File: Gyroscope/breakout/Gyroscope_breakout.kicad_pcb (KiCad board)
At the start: 2 copper layers, 30 x 22.9 mm, 5 parts, among them IC101 BMI088, J101 Conn_01x08

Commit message: Updated post review
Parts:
- C101, C102: footprint Gyroscope:C_0201_0603Metric -> Gyroscope:C_0805_2012Metric_Pad1.15x1.40mm_HandSolder
- moved C102 3.00 mm to (132.0, 98.1), turned to 0 degrees
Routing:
- net +3V3: track 32.8 -> 34.6 mm, vias 1 -> 2

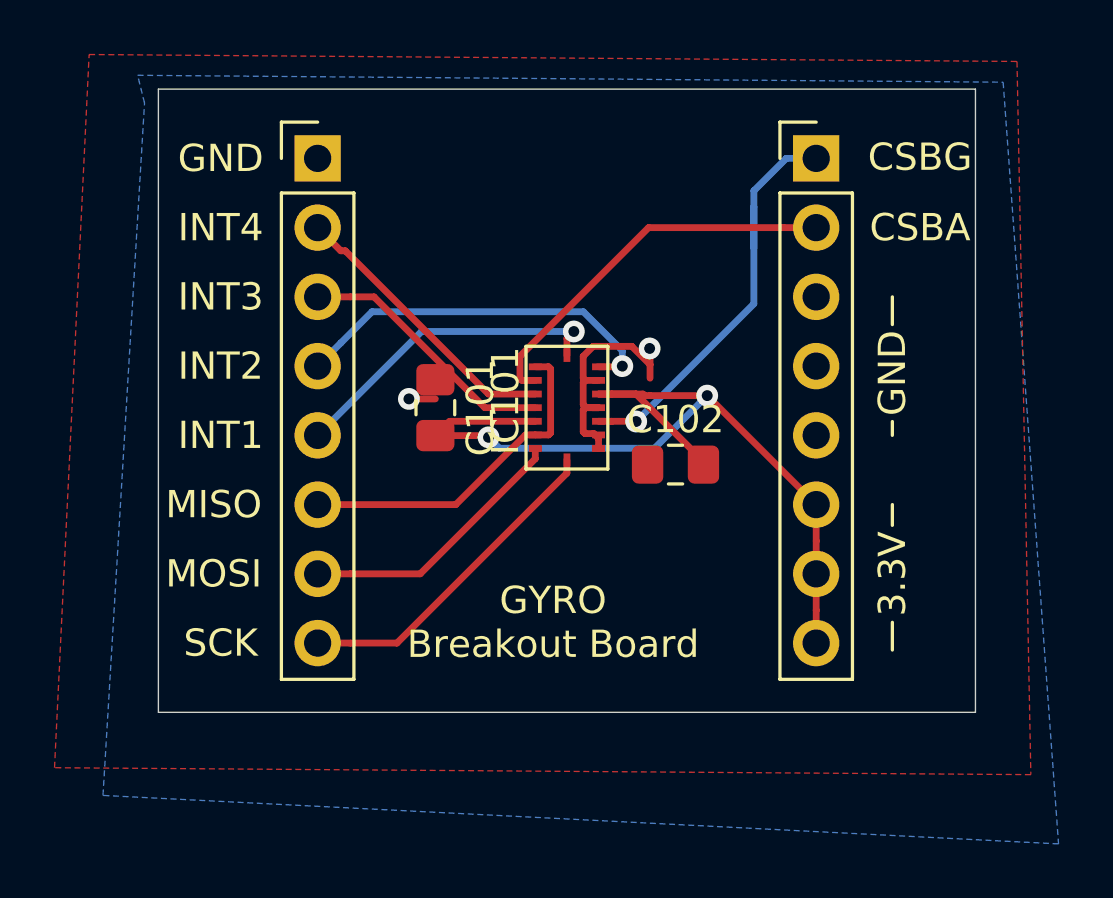
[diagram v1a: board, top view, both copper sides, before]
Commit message: Minor routing fix
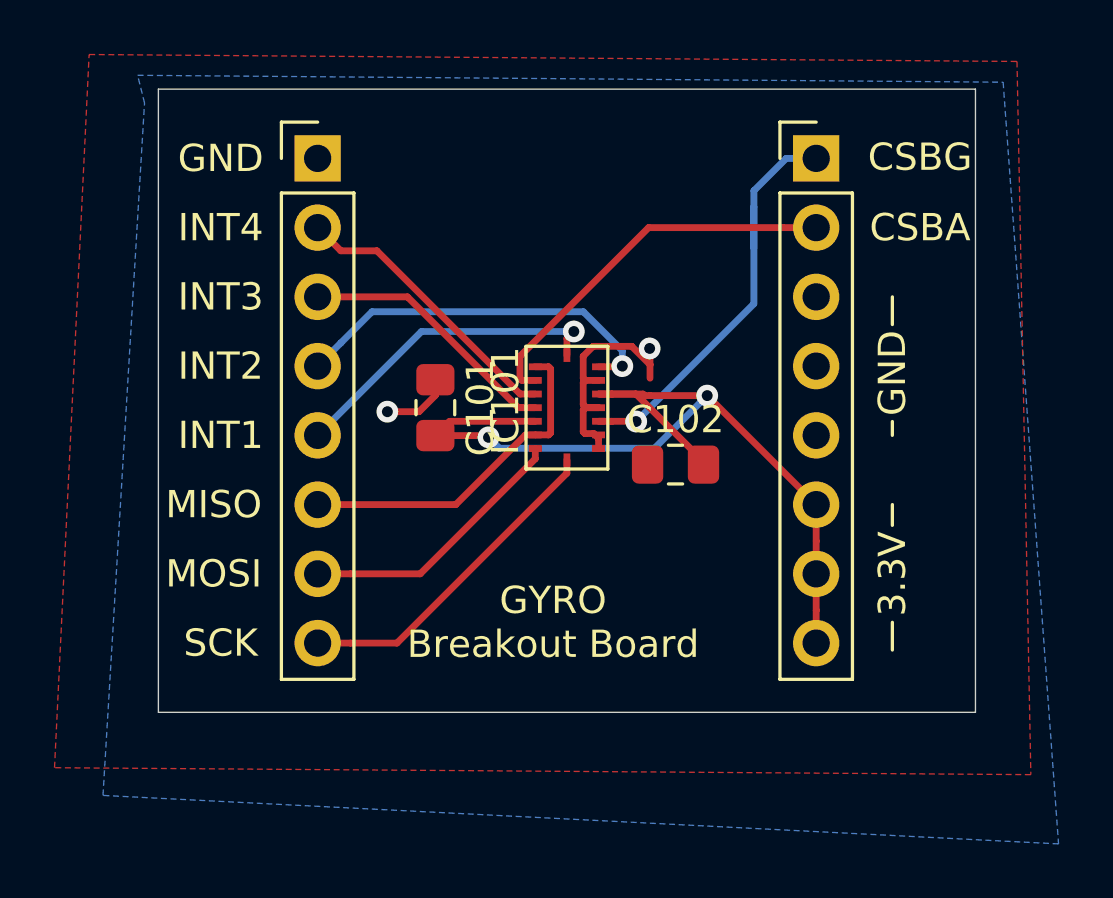
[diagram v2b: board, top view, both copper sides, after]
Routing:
- net GND: track 10.3 -> 11.9 mm
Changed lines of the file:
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@@
     (thickness 1.6)
     (drawings 21)
-    (tracks 99)
+    (tracks 100)
     (zones 0)
     (modules 5)
@@
   )
   (module Gyroscope:C_0805_2012Metric_Pad1.15x1.40mm_HandSolder (layer F.Cu)
+    (at 123.19 96.012 270)
+    (descr "Capacitor SMD 0805 (2012 Metric), square (rectangular) end terminal, IPC_7351 nominal with elongated pad for handsoldering. (Body size source: https://docs.google.com/spreadsheets/d/1BsfQQcO9C6DZCsRaXUlFlo91Tg2WpOkGARC1WS5S8t0/edit?usp=sharing), generated with kicad-footprint-generator")
+    (tags "capacitor handsolder")
+    (attr smd)
+    (fp_text reference C101 (at 0 -1.65 90) (layer F.SilkS)
+      (effects (font (size 1 1) (thickness 0.15)))
+    )
+    (fp_text value 100nF (at 0 1.65 90) (layer F.Fab)
+      (effects (font (size 1 1) (thickness 0.15)))
+    )
+    (fp_text user %R (at 0 0 90) (layer F.Fab)
+      (effects (font (size 0.5 0.5) (thickness 0.08)))
+    )
+    (fp_line (start 1.85 0.95) (end -1.85 0.95) (layer F.CrtYd) (width 0.05))
+    (fp_line (start 1.85 -0.95) (end 1.85 0.95) (layer F.CrtYd) (width 0.05))
+    (fp_line (start -1.85 -0.95) (end 1.85 -0.95) (layer F.CrtYd) (width 0.05))
+    (fp_line (start -1.85 0.95) (end -1.85 -0.95) (layer F.CrtYd) (width 0.05))
+    (fp_line (start -0.261252 0.71) (end 0.261252 0.71) (layer F.SilkS) (width 0.12))
+    (fp_line (start -0.261252 -0.71) (end 0.261252 -0.71) (layer F.SilkS) (width 0.12))
+    (fp_line (start 1 0.6) (end -1 0.6) (layer F.Fab) (width 0.1))
+    (fp_line (start 1 -0.6) (end 1 0.6) (layer F.Fab) (width 0.1))
+    (fp_line (start -1 -0.6) (end 1 -0.6) (layer F.Fab) (width 0.1))
+    (fp_line (start -1 0.6) (end -1 -0.6) (layer F.Fab) (width 0.1))
+    (pad 2 smd roundrect (at 1.025 0 270) (size 1.15 1.4) (layers F.Cu F.Paste F.Mask) (roundrect_rratio 0.217391)
+      (net 2 +3V3))
+    (pad 1 smd roundrect (at -1.025 0 270) (size 1.15 1.4) (layers F.Cu F.Paste F.Mask) (roundrect_rratio 0.217391)
+      (net 1 GND))
+    (model ${KISYS3DMOD}/Capacitor_SMD.3dshapes/C_0805_2012Metric.wrl
+      (at (xyz 0 0 0))
+      (scale (xyz 1 1 1))
+      (rotate (xyz 0 0 0))
+    )
+  )
+  (module Gyroscope:C_0805_2012Metric_Pad1.15x1.40mm_HandSolder (layer F.Cu)
     (at 132 98.1)
     (descr "Capacitor SMD 0805 (2012 Metric), square (rectangular) end terminal, IPC_7351 nominal with elongated pad for handsoldering. (Body size source: https://docs.google.com/spreadsheets/d/1BsfQQcO9C6DZCsRaXUlFlo91Tg2WpOkGARC1WS5S8t0/edit?usp=sharing), generated with kicad-footprint-generator")
@@
       (net 2 +3V3))
     (pad 1 smd roundrect (at -1.025 0) (size 1.15 1.4) (layers F.Cu F.Paste F.Mask) (roundrect_rratio 0.217391)
-      (net 1 GND))
-    (model ${KISYS3DMOD}/Capacitor_SMD.3dshapes/C_0805_2012Metric.wrl
-      (at (xyz 0 0 0))
-      (scale (xyz 1 1 1))
-      (rotate (xyz 0 0 0))
-    )
-  )
-  (module Gyroscope:C_0805_2012Metric_Pad1.15x1.40mm_HandSolder (layer F.Cu)
-    (at 123.19 96.012 270)
-    (descr "Capacitor SMD 0805 (2012 Metric), square (rectangular) end terminal, IPC_7351 nominal with elongated pad for handsoldering. (Body size source: https://docs.google.com/spreadsheets/d/1BsfQQcO9C6DZCsRaXUlFlo91Tg2WpOkGARC1WS5S8t0/edit?usp=sharing), generated with kicad-footprint-generator")
-    (tags "capacitor handsolder")
-    (attr smd)
-    (fp_text reference C101 (at 0 -1.65 90) (layer F.SilkS)
-      (effects (font (size 1 1) (thickness 0.15)))
-    )
-    (fp_text value 100nF (at 0 1.65 90) (layer F.Fab)
-      (effects (font (size 1 1) (thickness 0.15)))
-    )
-    (fp_text user %R (at 0 0 90) (layer F.Fab)
-      (effects (font (size 0.5 0.5) (thickness 0.08)))
-    )
-    (fp_line (start 1.85 0.95) (end -1.85 0.95) (layer F.CrtYd) (width 0.05))
-    (fp_line (start 1.85 -0.95) (end 1.85 0.95) (layer F.CrtYd) (width 0.05))
-    (fp_line (start -1.85 -0.95) (end 1.85 -0.95) (layer F.CrtYd) (width 0.05))
-    (fp_line (start -1.85 0.95) (end -1.85 -0.95) (layer F.CrtYd) (width 0.05))
-    (fp_line (start -0.261252 0.71) (end 0.261252 0.71) (layer F.SilkS) (width 0.12))
-    (fp_line (start -0.261252 -0.71) (end 0.261252 -0.71) (layer F.SilkS) (width 0.12))
-    (fp_line (start 1 0.6) (end -1 0.6) (layer F.Fab) (width 0.1))
-    (fp_line (start 1 -0.6) (end 1 0.6) (layer F.Fab) (width 0.1))
-    (fp_line (start -1 -0.6) (end 1 -0.6) (layer F.Fab) (width 0.1))
-    (fp_line (start -1 0.6) (end -1 -0.6) (layer F.Fab) (width 0.1))
-    (pad 2 smd roundrect (at 1.025 0 270) (size 1.15 1.4) (layers F.Cu F.Paste F.Mask) (roundrect_rratio 0.217391)
-      (net 2 +3V3))
-    (pad 1 smd roundrect (at -1.025 0 270) (size 1.15 1.4) (layers F.Cu F.Paste F.Mask) (roundrect_rratio 0.217391)
       (net 1 GND))
     (model ${KISYS3DMOD}/Capacitor_SMD.3dshapes/C_0805_2012Metric.wrl
@@
   (segment (start 131.064 94.430998) (end 131.064 93.854) (width 0.25) (layer F.Cu) (net 1))
   (segment (start 131.064 93.854) (end 131.05 93.84) (width 0.25) (layer F.Cu) (net 1))
-  (segment (start 122.222 95.692) (end 122.22 95.69) (width 0.25) (layer F.Cu) (net 1))
-  (via (at 122.22 95.69) (size 0.8) (drill 0.4) (layers F.Cu B.Cu) (net 1))
-  (segment (start 123.19 95.692) (end 122.222 95.692) (width 0.25) (layer F.Cu) (net 1) (status 10))
+  (via (at 121.43 96.16) (size 0.8) (drill 0.4) (layers F.Cu B.Cu) (net 1))
+  (segment (start 122.592 96.16) (end 121.43 96.16) (width 0.25) (layer F.Cu) (net 1))
+  (segment (start 123.19 94.987) (end 123.19 95.562) (width 0.25) (layer F.Cu) (net 1))
+  (segment (start 123.19 95.562) (end 122.592 96.16) (width 0.25) (layer F.Cu) (net 1))
   (segment (start 130.806 95.512) (end 129.176 95.512) (width 0.25) (layer F.Cu) (net 2) (status 20))
   (segment (start 131.064 95.57) (end 130.864 95.57) (width 0.25) (layer F.Cu) (net 2) (status 30))
@@
   (segment (start 126.494178 97.012) (end 126.856 97.012) (width 0.25) (layer F.Cu) (net 7))
   (segment (start 118.872 99.568) (end 123.938178 99.568) (width 0.25) (layer F.Cu) (net 7))
-  (segment (start 120.940002 91.948) (end 120.074081 91.948) (width 0.25) (layer F.Cu) (net 8))
-  (segment (start 125.004002 96.012) (end 120.940002 91.948) (width 0.25) (layer F.Cu) (net 8))
-  (segment (start 120.074081 91.948) (end 118.872 91.948) (width 0.25) (layer F.Cu) (net 8) (status 20))
-  (segment (start 126.856 96.012) (end 125.004002 96.012) (width 0.25) (layer F.Cu) (net 8) (status 10))
-  (segment (start 119.721999 90.257999) (end 118.872 89.408) (width 0.25) (layer F.Cu) (net 9) (status 20))
-  (segment (start 125.140412 95.512) (end 119.886411 90.257999) (width 0.25) (layer F.Cu) (net 9))
-  (segment (start 119.886411 90.257999) (end 119.721999 90.257999) (width 0.25) (layer F.Cu) (net 9))
-  (segment (start 126.856 95.512) (end 125.140412 95.512) (width 0.25) (layer F.Cu) (net 9) (status 10))
+  (segment (start 126.3685 96.012) (end 126.856 96.012) (width 0.25) (layer F.Cu) (net 8))
+  (segment (start 126.230315 96.012) (end 126.3685 96.012) (width 0.25) (layer F.Cu) (net 8))
+  (segment (start 122.166315 91.948) (end 126.230315 96.012) (width 0.25) (layer F.Cu) (net 8))
+  (segment (start 118.872 91.948) (end 122.166315 91.948) (width 0.25) (layer F.Cu) (net 8))
+  (segment (start 119.721999 90.257999) (end 118.872 89.408) (width 0.25) (layer F.Cu) (net 9))
+  (segment (start 121.045406 90.257999) (end 119.721999 90.257999) (width 0.25) (layer F.Cu) (net 9))
+  (segment (start 126.299407 95.512) (end 121.045406 90.257999) (width 0.25) (layer F.Cu) (net 9))
+  (segment (start 126.856 95.512) (end 126.299407 95.512) (width 0.25) (layer F.Cu) (net 9))
   (segment (start 135.957919 89.408) (end 137.16 89.408) (width 0.25) (layer F.Cu) (net 10) (status 20))
   (segment (start 131.012498 89.408) (end 135.957919 89.408) (width 0.25) (layer F.Cu) (net 10))

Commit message: adjusted gyro soldermask
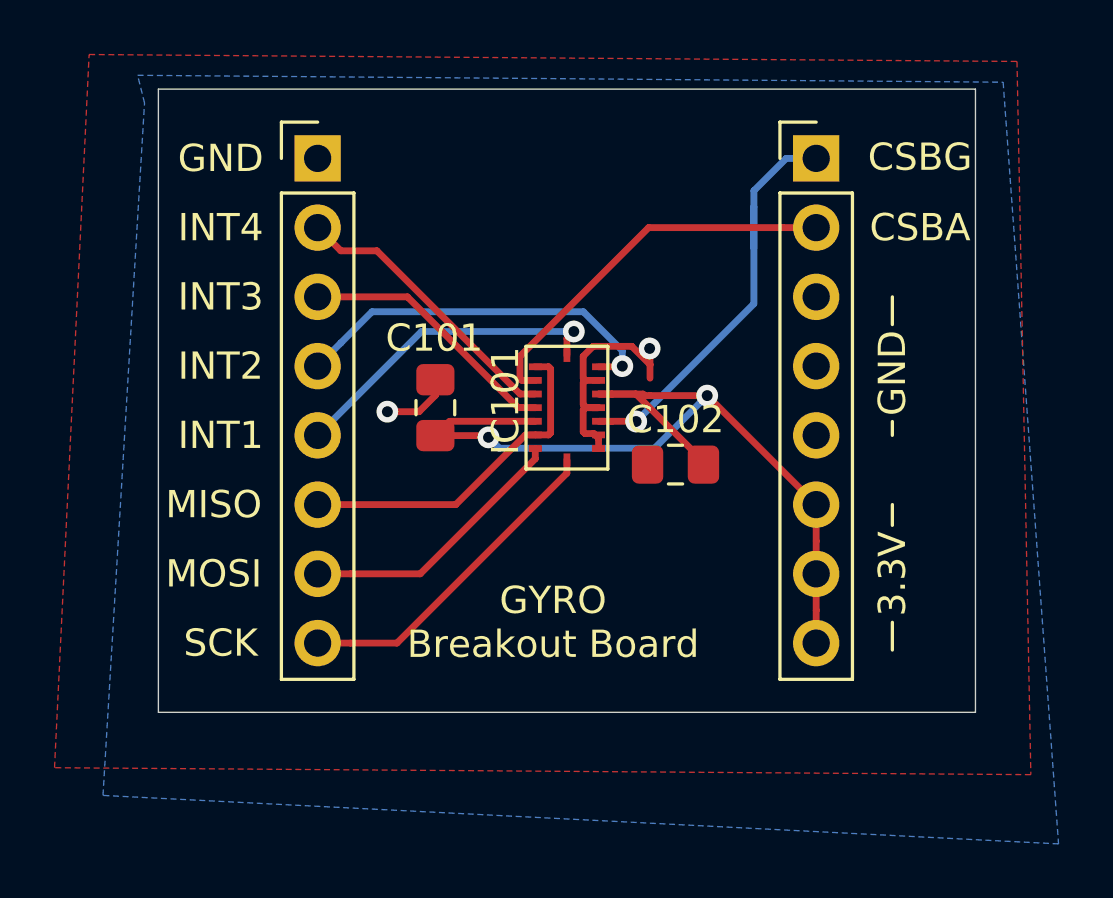
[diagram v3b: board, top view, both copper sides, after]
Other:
- rule pad_to_mask_clearance: 0.051 -> 0.0508
